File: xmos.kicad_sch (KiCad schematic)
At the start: 84 parts, among them J3 XTAG DEV, J4 XMOS JTAG, Q1 LBSS138WT1G, Q2 LBSS138WT1G, Q3 BC847B, U10 XU316-1024-QF60B-C24​, U11 W25Q32JVSSIQ, U12 SN74LVC125APWR, U13 TLV73333PDBVR, X1 24MHz 12pF

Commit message: Publish KiCad 10 hardware updates
Refresh the Nest Mini v2 drop-in PCB project in KiCad 10 and publish the accumulated schematic and board updates as a single clean mainline change.

Remove the unused USB-C power/input branch from the power sheet, including the USB connector path, data switching, VBUS switching, and associated support parts, while preserving the pogo-accessible USB signals where needed. Add the ESP32-C6 1x05 pogo connector with the J2-style pin order for GND, boot, reset, USB D-, and USB D+ without a 3.3 V pin.

Add a 5 V SN74AHCT1G125 buffer for the LED data input, with local decoupling and a 47 ohm series output resistor, so the LED chain receives a buffered LED_WS2812_5V signal from the ESP_WS2812 control net.

Carry forward the KiCad 10 project save state and schematic cleanups for the XMOS, ESP32, audio, LED, and power sheets without changing the TAS amplifier topology.
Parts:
- renumbered C42 to C56, C43 to C57, C44 to C58, C45 to C59, C46 to C60, C47 to C61, C48 to C62, C49 to C63, C50 to C64, C51 to C65, C52 to C66, C53 to C67, C54 to C68, C55 to C69, C56 to C70, C57 to C71, C58 to C72, C59 to C73, C60 to C74, C61 to C75, C62 to C76, C63 to C77, C64 to C78, C65 to C79, C66 to C80, C67 to C81, C68 to C82, C69 to C83, C70 to C84, C71 to C85, C72 to C86, C73 to C87, D6 to D3, R34 to R35, R35 to R36, R36 to R37, R37 to R38, R38 to R39, R39 to R40, R40 to R41, R41 to R42, R42 to R43, R43 to R44, R44 to R45, R45 to R46, R46 to R47, R47 to R48, R48 to R49, R49 to R50, R50 to R51, R51 to R52, R52 to R53, R53 to R54, R54 to R55, R55 to R56, R56 to R57, R57 to R58, R58 to R59, R59 to R60, R60 to R61, R61 to R62, R62 to R63, R63 to R64, R64 to R65, R65 to R66, TP12 to TP10, TP10 to TP8, TP11 to TP9, U11 to U10, U12 to U11, U13 to U12, U10 to U9
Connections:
- net MIC_DATA_M_2: now also U11.2 (1A); no longer U11.1 (1~{OE})
- net MUTE_ON: now also U11.1 (1~{OE}); no longer U11.2 (1A)
- net I2C2_SCL: no longer names the net of U9.40 (X0D29)
- net I2C2_SDA: no longer names the net of U9.54 (X0D30)
- net XMOS_USB_N: no longer names the net of U9.28 (USB_DM)
- net XMOS_USB_P: no longer names the net of U9.29 (USB_DP)
- no-connect marks 10 -> 14
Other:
- moved on the sheet: R52

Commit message: Publish ESP32-P4 multi-sheet hardware redesign
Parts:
- removed C60, C61, C63, C64, C65, C66, C69, C70, C71, C73, C74, C80: 100nF, Capacitor_SMD:C_0402_1005Metric, symbol Device:C
- removed C62, C68: 20pF, Capacitor_SMD:C_0402_1005Metric, symbol Seeed_libdb:Capacitors/302010050
- removed C67: 1uF, Capacitor_SMD:C_0402_1005Metric, symbol Seeed_libdb:Capacitors/302013249
- removed C75, C76, C77: 100nF, Capacitor_SMD:C_0402_1005Metric, symbol Seeed_libadl:Capacitors/302010024
- removed FB3: 600R, Onju:BLM18PG121SN1D, symbol Device:FerriteBead
- removed FB4: 120R, Onju:BLM18PG121SN1D, symbol Device:FerriteBead
- removed FB5: 600R, Onju:BLM18PG121SN1D, symbol Seeed_libadl:Ferrite Bead/303030521
- removed J3: XTAG DEV, Connector_PinHeader_2.54mm:PinHeader_1x04_P2.54mm_Vertical, symbol Connector:Conn_01x04_Pin
- removed J4: XMOS JTAG, Connector_PinHeader_2.54mm:PinHeader_2x05_P2.54mm_Vertical, symbol Connector_Generic_MountingPin:Conn_2Rows-09Pins_MountingPin
- removed Q1: LBSS138WT1G, Onju:SC-70-3_L2.1-W1.3-P0.65-LS2.1-BR, symbol New_Library:LBSS138WT1G
- removed Q2: LBSS138WT1G, Package_TO_SOT_SMD:SOT-323_SC-70, symbol Seeed_libadl:Mosfet/305031542
- removed R35: 1M, Resistor_SMD:R_0402_1005Metric, symbol Seeed_libadl:Resistors/301010009
- removed R36: 680R, Resistor_SMD:R_0402_1005Metric, symbol Seeed_libadl:Resistors/301010505
- removed R37: 47k, Resistor_SMD:R_0402_1005Metric, symbol Device:R
- removed R38, R39: 22R, Resistor_SMD:R_0402_1005Metric, symbol Seeed_libdb:Resistors/301010002
- removed R40: 100R, Resistor_SMD:R_0402_1005Metric, symbol Seeed_libdb:Resistors/301010028
- removed R41, R43, R44, R45, R46, R47: 0R, Resistor_SMD:R_0402_1005Metric, symbol Seeed_libdb:Resistors/301010000
- removed R42: 100k, Resistor_SMD:R_0402_1005Metric, symbol Device:R
- removed R48: 100R, Resistor_SMD:R_0402_1005Metric, symbol Seeed_libadl:Resistors/301010028
- removed R49: 470k, Resistor_SMD:R_0402_1005Metric, symbol Seeed_libdb:Resistors/301010069
- removed R50: 10k, Resistor_SMD:R_0402_1005Metric, symbol Seeed_libadl:Resistors/301010047
- removed R51: 4.7k, Resistor_SMD:R_0402_1005Metric, symbol Device:R
- removed TP8: TEST-POINT, TestPoint:TestPoint_Pad_D1.0mm, symbol 0_Seeed_Misc:TEST-POINT
- removed TP9: XU316_RST, TestPoint:TestPoint_Pad_D1.0mm, symbol Connector:TestPoint
- removed U10: W25Q32JVSSIQ, Package_SO:SOIC-8_5.3x5.3mm_P1.27mm, symbol Memory_Flash:W25Q128JVS
- removed U9: XU316-1024-QF60B-C24​, Onju:XU316-1024-QF60B-C24, symbol reSpeaker:XU316-1024-QF60A-C24​
- removed X1: 24MHz 12pF, Onju:X4-SMD-2.0X1.6MM, symbol Seeed_libdb:OSC & XTAL/306011444
- added C113, C114, C116, C117, C118: 1uF, Capacitor_SMD:C_0402_1005Metric, symbol Device:C
- added C115, C119, C121, C122, C123, C124, C125, C126, C127, C129, C130, C131, C132, C134, C135, C137, C139, C44: 100nF, Capacitor_SMD:C_0402_1005Metric, symbol Device:C
- added C120, C128, C136, C138: 10uF, Capacitor_SMD:C_0603_1608Metric, symbol Device:C
- added C133: 10nF, Capacitor_SMD:C_0402_1005Metric, symbol Device:C
- added C9: 4.7uF, Capacitor_SMD:C_0603_1608Metric, symbol Device:C
- added D4: LRB520S-30T1G, Diode_SMD:D_SOD-523, symbol Device:D
- added J3: P4 PROGRAM POGO, Connector_PinHeader_2.54mm:PinHeader_1x05_P2.54mm_Vertical, symbol Connector_Generic:Conn_01x05
- added R32, R35, R74: 10k, Resistor_SMD:R_0402_1005Metric, symbol Device:R
- added U4: (no value), Espressif:ESP32-P4, symbol Espressif:ESP32-P4X
- added U9: W25Q128JVSIQ, Package_SO:SOIC-8_5.3x5.3mm_P1.27mm, symbol Memory_Flash:W25Q128JVS
- added Y3: 40MHz, Crystal:Crystal_SMD_2016-4Pin_2.0x1.6mm, symbol Device:Crystal_GND24
- C56, C57: value 100nF -> 12pF; Dielectric X7R -> NP0; Function XMOS -> ESP32-P4; LCSC Part # C1525 -> C1547; MPN (none) -> 0402CG120J500NT; Manufacturer Samsung Electro-Mechanics -> FH (Guangdong Fenghua Advanced Tech); Manufacturer Part CL05B104KO5NNNC -> 0402CG120J500NT; Supplier Part C1525 -> (none); Voltage 16V -> 50V
- C58: footprint Capacitor_SMD:C_0402_1005Metric -> Capacitor_SMD:C_0603_1608Metric; Function XMOS -> ESP32-P4; Supplier Part C52923 -> (none)
- C59: value 100nF -> 12pF; Dielectric X7R -> NP0; Function XMOS -> ESP32-P4; LCSC Part # C1525 -> C1547; MPN (none) -> 0402CG120J500NT; Manufacturer Samsung Electro-Mechanics -> FH (Guangdong Fenghua Advanced Tech); Manufacturer Part CL05B104KO5NNNC -> 0402CG120J500NT; Supplier Part C1525 -> C1547; Voltage 16V -> 50V
- C72: Function XMOS -> ESP32-P4
- C81, R56, R58: Function XMOS -> MIC
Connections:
- net ESP_3V3: now also C119.1, C120.1, C122.1, C123.1, C127.1, C128.1, C129.1, C130.1, C132.1, C133.1, C134.1, C137.1, C138.1, C139.1, C9.1, D4.1 (K), R32.1, R35.1, U4.101 (VDD_ANA), U4.102 (VDD_BAT), U4.21 (VDD_IO_0), U4.51 (VDD_USBPHY), U4.62 (VDD_IO_4), U4.75 (VDD_LDO), U4.77 (VDD_DCDCC), U4.85 (VDD_IO_5), U4.9 (VDD_LP), U4.96 (VDD_IO_6)
- net GND: now also C56.1, C57.1, C113.2, C114.2, C115.2, C116.2, C117.2, C118.2, C119.2, C120.2, C121.2, C122.2, C123.2, C124.2, C125.2, C126.2, C127.2, C128.2, C129.2, C130.2, C131.2, C132.2, C133.2, C134.2, C135.2, C136.2, C137.2, C138.2, C139.2, C44.2, C9.2, J3.1 (Pin_1), U4.105 (GND), U9.4 (GND), Y3.2, Y3.4; no longer C56.2, C57.2
- removed net +1V8: C56.1, C57.1, C59.1
- net VDD renamed P4_RST
- net P4_RST: now also D4.2 (A), J3.3 (Pin_3), R32.2, U4.103 (CHIP_PU)
- new net: C57.2, U4.99 (XTAL_N), Y3.1
- new net: C56.2, U4.100 (XTAL_P), Y3.3
- new net EN_DCDC: U4.79 (EN_DCDC)
- new net ESP_VDD_HP: C121.1, C126.1, C131.1, C135.1, C136.1, U4.26 (VDD_HP_0), U4.54 (VDD_HP_1), U4.76 (VDD_HP_2), U4.91 (VDD_HP_3)
- new net FB_DCDC: U4.78 (FB_DCDC)
- new net P4_BOOT: C59.1, J3.2 (Pin_2), R35.2, U4.104 (GPIO0)
- new net P4_USB_N: J3.4 (Pin_4), U4.49 (USB-DM)
- new net P4_USB_P: J3.5 (Pin_5), U4.50 (USB-DP)
- new net SPI_CLK: U4.32 (FLASH_CK), U9.6 (CLK)
- new net SPI_CS0: R74.2, U4.27 (FLASH_CS), U9.1 (~{CS})
- new net SPI_D: U4.33 (FLASH_D), U9.5 (DI/IO_{0})
- new net SPI_HD: U4.31 (FLASH_HOLD), U9.7 (~{HOLD}/~{RESET}/IO_{3})
- new net SPI_Q: U4.28 (FLASH_Q), U9.2 (DO/IO_{1})
- new net SPI_WP: U4.29 (FLASH_WP), U9.3 (~{WP}/IO_{2})
- new net VDDO_3: C117.1, U4.73 (VDDO_3)
- new net VDDO_4: C118.1, U4.74 (VDDO_4)
- new net VDDO_FLASH: C113.1, C114.1, C115.1, C44.1, R74.1, U4.30 (VDD_FLASH_IO), U4.71 (VDDO_FLASH), U9.8 (VCC)
- new net VDDO_PSRAM: C116.1, C124.1, C125.1, U4.59 (VDD_PSRAM_0), U4.67 (VDD_PSRAM_1), U4.72 (VDDO_PSRAM)
- no-connect marks 14 -> 65
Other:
- moved on the sheet: C72, C84, D3, R52, R53, R57, R59, U11

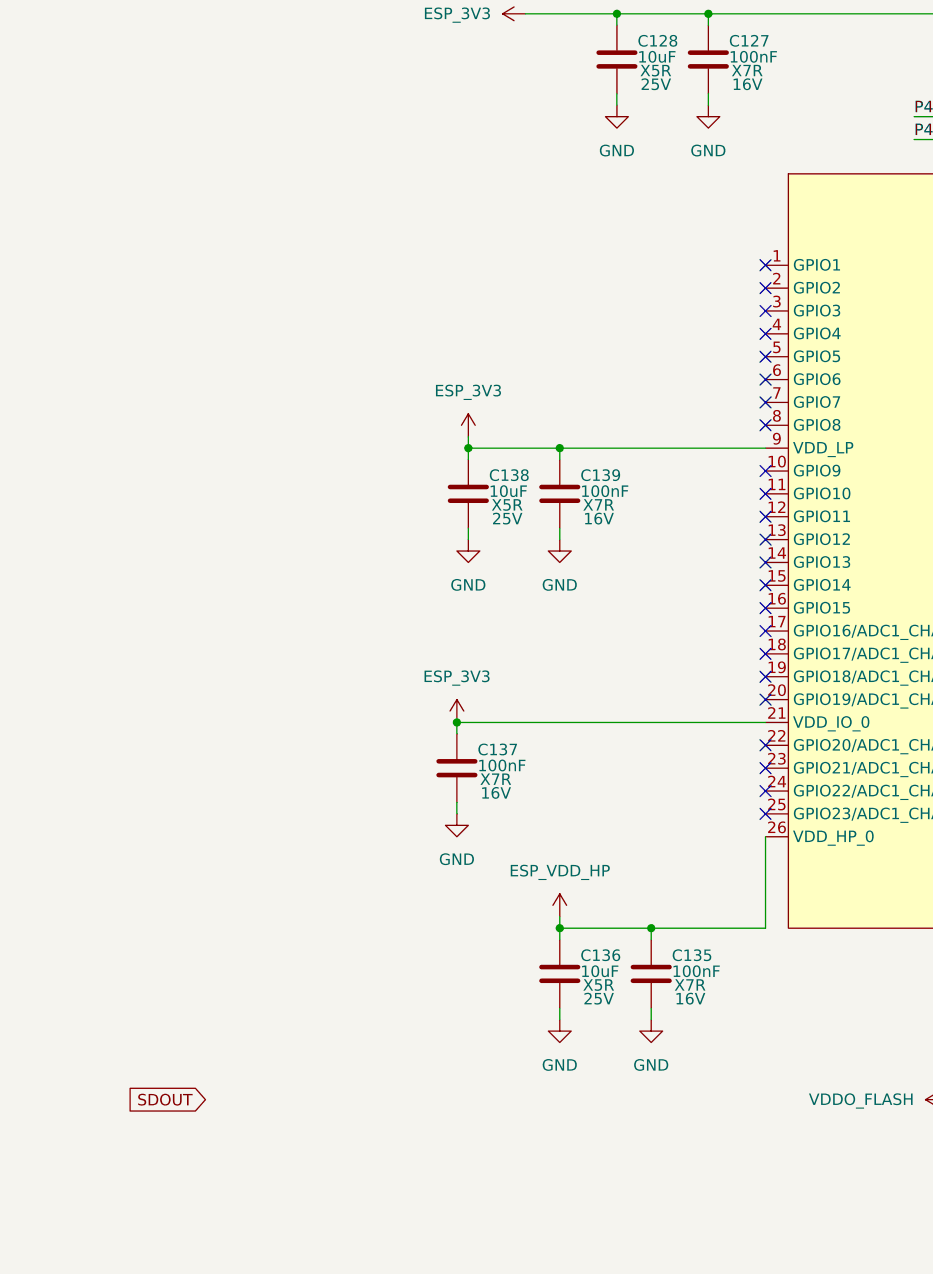
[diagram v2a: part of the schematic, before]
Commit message: Update KiCad schematics and PCB layout
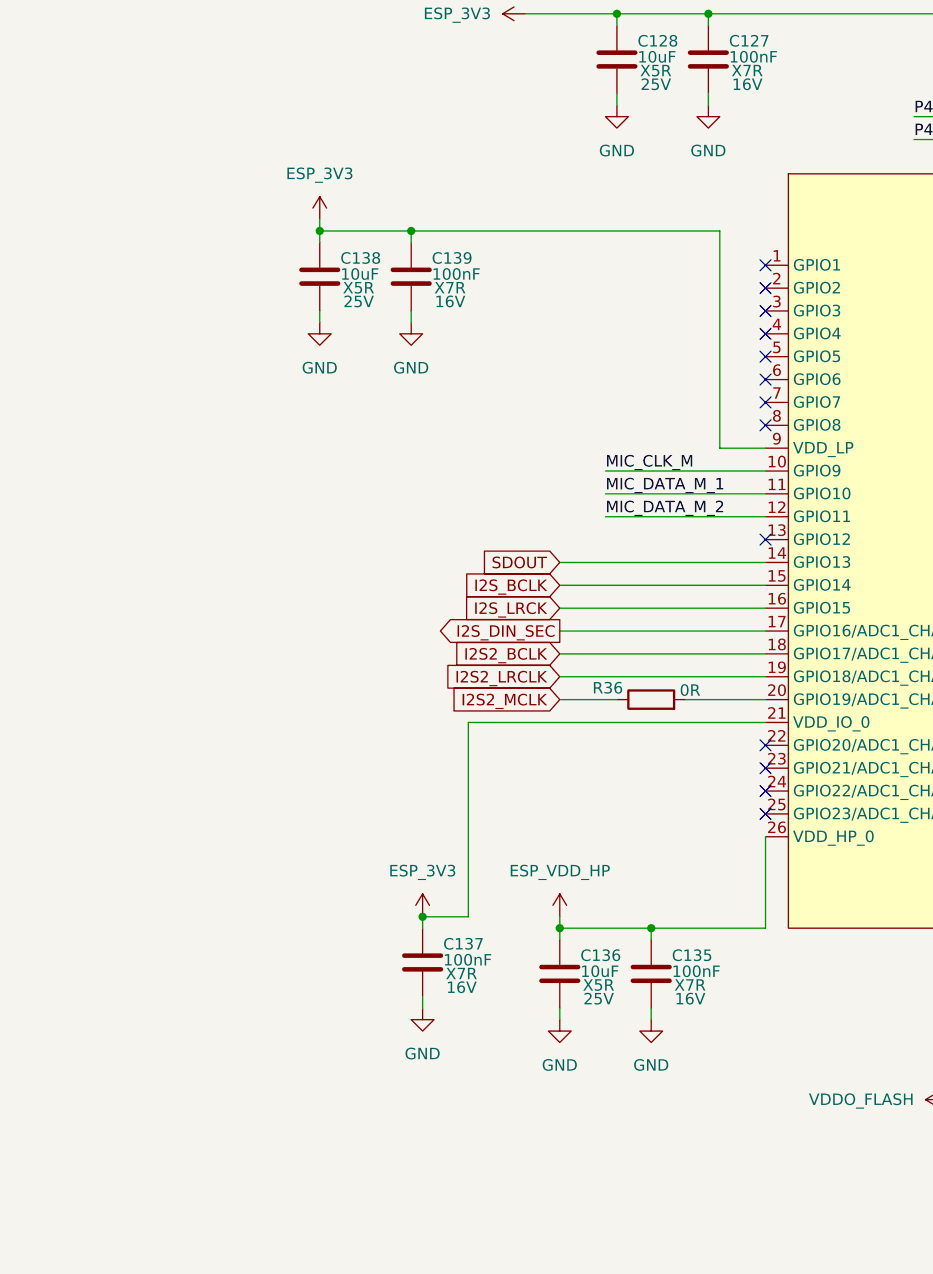
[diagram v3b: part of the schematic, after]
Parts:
- added R36: 0R, Resistor_SMD:R_0402_1005Metric, symbol Device:R
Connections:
- net MIC_CLK_M: now also U4.10 (GPIO9)
- net MIC_DATA_M_1: now also U4.11 (GPIO10)
- net MIC_DATA_M_2: now also U4.12 (GPIO11)
- net SDOUT: now also U4.14 (GPIO13)
- net I2S_BCLK: now reaches U4.15 (GPIO14)
- net I2S_LRCK: now reaches U4.16 (GPIO15)
- net I2S_DIN_SEC: now reaches U4.17 (GPIO16/ADC1_CHANNEL0)
- net I2S2_BCLK: now reaches U4.18 (GPIO17/ADC1_CHANNEL1)
- net I2S2_LRCLK: now reaches U4.19 (GPIO18/ADC1_CHANNEL2)
- net at U4.20 (GPIO19/ADC1_CHANNEL3): now also R36.2
- new net I2S2_MCLK: R36.1
- no-connect marks 65 -> 55
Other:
- moved on the sheet: C137, C138, C139
